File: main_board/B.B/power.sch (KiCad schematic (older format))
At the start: 38 parts

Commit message: konzultace_s_Kubou_01
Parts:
- removed C? (x7): 10uf, Capacitor_SMD:C_0805_2012Metric, symbol Device:C
- removed C? (x3): 2.2uf, Capacitor_SMD:C_0805_2012Metric, symbol Device:C
- removed C? (x4): 22uf, Capacitor_SMD:C_0805_2012Metric, symbol Device:C
- removed C? (x6): 4.7uf, Capacitor_SMD:C_0805_2012Metric, symbol Device:C
- removed C? (x3): 0.1uf, Capacitor_SMD:C_0402_1005Metric, symbol Device:C
- removed L? (x2): 4,7uH, symbol Device:L
- removed L?: 1.5uh, symbol Device:L
- removed R? (x3): 100k, Resistor_SMD:R_0402_1005Metric, symbol Device:R
- removed R?: 33k, Resistor_SMD:R_0402_1005Metric, symbol Device:R
- removed R?: 7.5k, Resistor_SMD:R_0402_1005Metric, symbol Device:R
- removed R?: 150k, Resistor_SMD:R_0402_1005Metric, symbol Device:R
- removed R?: 20k, Resistor_SMD:R_0402_1005Metric, symbol Device:R
- removed R?: 56k, Resistor_SMD:R_0402_1005Metric, symbol Device:R
- removed R?: 10k, Resistor_SMD:R_0402_1005Metric, symbol Device:R
- removed U? (x2): FR9885, Package_TO_SOT_SMD:SOT-23-6, symbol B.B-rescue:FR9885
- removed U?: SY8286A, Package_DFN_QFN:QFN-20-1EP_4x4mm_P0.5mm_EP2.7x2.7mm, symbol B.B-rescue:SY8286A
- added C? (x3): 10uf, Capacitor_SMD:C_0805_2012Metric, symbol Device:C
- added C? (x3): 2.2uf, Capacitor_SMD:C_0805_2012Metric, symbol Device:C
- added C?: 4.7uf, Capacitor_SMD:C_0805_2012Metric, symbol Device:C
- added C? (x4): 22uf, Capacitor_SMD:C_0805_2012Metric, symbol Device:C
- added C?: 100nf, Capacitor_SMD:C_0402_1005Metric, symbol Device:C
- added C?: 10nf, Capacitor_SMD:C_0402_1005Metric, symbol Device:C
- added C?: 47nf, Capacitor_SMD:C_0402_1005Metric, symbol Device:C
- added C?: 10pf, Capacitor_SMD:C_0402_1005Metric, symbol Device:C
- added C?: 1nf, Capacitor_SMD:C_0402_1005Metric, symbol Device:C
- added C?: 1uf, Capacitor_SMD:C_0402_1005Metric, symbol Device:C
- added D? (x2): D_Schottky, symbol Device:D_Schottky
- added L? (x2): 2.2uH, symbol Device:L
- added Q? (x2): Q_NMOS_DSG, symbol Device:Q_NMOS_DSG
- added R?: 150k, Resistor_SMD:R_0402_1005Metric, symbol Device:R
- added R?: 20k, Resistor_SMD:R_0402_1005Metric, symbol Device:R
- added R? (x3): 100k, Resistor_SMD:R_0402_1005Metric, symbol Device:R
- added R?: 33k, Resistor_SMD:R_0402_1005Metric, symbol Device:R
- added R? (x2): 7.5k, Resistor_SMD:R_0402_1005Metric, symbol Device:R
- added R?: 10, Resistor_SMD:R_0402_1005Metric, symbol Device:R
- added R?: 1.5, Resistor_SMD:R_0402_1005Metric, symbol Device:R
- added U?: AOZ1280, Package_TO_SOT_SMD:SOT-23-6, symbol B.B-rescue:AOZ1280
- added U?: FP6296, symbol B.B-rescue:FP6296
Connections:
- net labels removed: 4V, NC, SHUTDOWN_4V, low_power_3V3
- wire segments 105 -> 76
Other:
- note removed: "low power 3V3 output can provide \nmax continuous current 150mA"

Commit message: preparation_to_drawing_PCB
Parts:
- removed D?: D_Schottky, symbol Device:D_Schottky
- removed Q? (x2): Q_NMOS_DSG, symbol Device:Q_NMOS_DSG
- added D?: D_Schottky, BB:DO-214AC, symbol Device:D_Schottky
- added Q? (x2): CJ3134K, Package_TO_SOT_SMD:SOT-23, symbol Transistor_FET:2N7002
- C?: LCSC (none) -> C1525
- C?: value 47nf -> 33nf; LCSC (none) -> C1585
- C?: LCSC (none) -> C32949
- C?: LCSC (none) -> C1523
- C?: LCSC (none) -> C52923
- D?: footprint (none) -> BB:DO-214AC; LCSC (none) -> C22452
- L?: footprint (none) -> BB:SMD-PIND-10.5x11.5x4_2.5x3.0; LCSC (none) -> C149550
- L?: value 2.2uH -> 3.3uH; footprint (none) -> BB:SMD-PIND-12.8x13.5x5_2.0x5.0; LCSC (none) -> C149571
- R?: value 150k -> 100k; LCSC C25755 -> C25741
- R?: value 20k -> 33k; LCSC C25765 -> C25779
- R?: LCSC C25755 -> C25077
- R?: LCSC (none) -> C270642
- U?: footprint (none) -> Package_SO:SOP-8_3.76x4.96mm_P1.27mm; LCSC (none) -> C133888
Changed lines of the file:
@@
 F 0 "L?" V 6590 2350 50  0000 C CNN
 F 1 "2.2uH" V 6499 2350 50  0000 C CNN
-F 2 "" H 6400 2350 50  0001 C CNN
+F 2 "BB:SMD-PIND-10.5x11.5x4_2.5x3.0" H 6400 2350 50  0001 C CNN
 F 3 "~" H 6400 2350 50  0001 C CNN
+F 4 "C149550" V 6400 2350 50  0001 C CNN "LCSC"
 	1    6400 2350
 	0    -1   -1   0
@@
 	4900 2400 4950 2400
 $Comp
-L Device:Q_NMOS_DSG Q?
-U 1 1 5FA82314
-P 4800 2950
-AR Path="/5F9EE529/5FA82314" Ref="Q?"  Part="1"
-AR Path="/5FA9DBB3/5FA82314" Ref="Q?"  Part="1"
-AR Path="/5FA4C94D/5FA82314" Ref="Q?"  Part="1"
-F 0 "Q?" H 5004 2996 50  0000 L CNN
-F 1 "Q_NMOS_DSG" H 5004 2905 50  0000 L CNN
-F 2 "" H 5000 3050 50  0001 C CNN
-F 3 "~" H 4800 2950 50  0001 C CNN
-	1    4800 2950
-	1    0    0    -1
-$EndComp
-$Comp
 L B.B-eagle-import:GND #GND?
 U 1 1 5FA8231A
@@
 F 0 "D?" V 6154 2729 50  0000 L CNN
 F 1 "D_Schottky" V 6245 2729 50  0000 L CNN
-F 2 "" H 6200 2650 50  0001 C CNN
+F 2 "BB:DO-214AC" H 6200 2650 50  0001 C CNN
 F 3 "~" H 6200 2650 50  0001 C CNN
+F 4 "C22452" V 6200 2650 50  0001 C CNN "LCSC"
 	1    6200 2650
 	0    1    1    0
@@
 F 0 "U?" H 5250 4625 50  0000 C CNN
 F 1 "FP6296" H 5250 4534 50  0000 C CNN
-F 2 "" H 5250 4400 50  0001 C CNN
+F 2 "Package_SO:SOP-8_3.76x4.96mm_P1.27mm" H 5250 4400 50  0001 C CNN
 F 3 "" H 5250 4400 50  0001 C CNN
+F 4 "C133888" H 5250 4400 50  0001 C CNN "LCSC"
 	1    5250 4400
 	1    0    0    -1
@@
 AR Path="/5F9AAC80/5FA6804A" Ref="R?"  Part="1"
 F 0 "R?" H 6870 4246 50  0000 L CNN
-F 1 "150k" H 6870 4155 50  0000 L CNN
+F 1 "100k" H 6870 4155 50  0000 L CNN
 F 2 "Resistor_SMD:R_0402_1005Metric" V 6730 4200 50  0001 C CNN
 F 3 "~" H 6800 4200 50  0001 C CNN
-F 4 "C25755" H 6800 4200 50  0001 C CNN "LCSC"
+F 4 "C25741" H 6800 4200 50  0001 C CNN "LCSC"
 	1    6800 4200
 	1    0    0    -1
@@
 AR Path="/5F9AAC80/5FA68052" Ref="R?"  Part="1"
 F 0 "R?" H 6870 4546 50  0000 L CNN
-F 1 "20k" H 6870 4455 50  0000 L CNN
+F 1 "33k" H 6870 4455 50  0000 L CNN
 F 2 "Resistor_SMD:R_0402_1005Metric" V 6730 4500 50  0001 C CNN
 F 3 "~" H 6800 4500 50  0001 C CNN
-F 4 "C25765" H 6800 4500 50  0001 C CNN "LCSC"
+F 4 "C25779" H 6800 4500 50  0001 C CNN "LCSC"
 	1    6800 4500
 	1    0    0    -1
@@
 P 4350 4000
 F 0 "L?" V 4540 4000 50  0000 C CNN
-F 1 "2.2uH" V 4449 4000 50  0000 C CNN
-F 2 "" H 4350 4000 50  0001 C CNN
+F 1 "3.3uH" V 4449 4000 50  0000 C CNN
+F 2 "BB:SMD-PIND-12.8x13.5x5_2.0x5.0" H 4350 4000 50  0001 C CNN
 F 3 "~" H 4350 4000 50  0001 C CNN
+F 4 "C149571" V 4350 4000 50  0001 C CNN "LCSC"
 	1    4350 4000
 	0    -1   -1   0
-$EndComp
-$Comp
-L Device:D_Schottky D?
-U 1 1 5FA8F317
-P 5250 4000
-F 0 "D?" H 5200 3800 50  0000 L CNN
-F 1 "D_Schottky" H 5050 3900 50  0000 L CNN
-F 2 "" H 5250 4000 50  0001 C CNN
-F 3 "~" H 5250 4000 50  0001 C CNN
-	1    5250 4000
-	-1   0    0    1
 $EndComp
 $Comp
@@
 F 2 "Capacitor_SMD:C_0402_1005Metric" H 5888 4250 50  0001 C CNN
 F 3 "~" H 5850 4400 50  0001 C CNN
-F 4 "" V 5850 4400 50  0001 C CNN "LCSC"
+F 4 "C1525" V 5850 4400 50  0001 C CNN "LCSC"
 	1    5850 4400
 	0    1    1    0
@@
 F 2 "Resistor_SMD:R_0402_1005Metric" V 5580 4200 50  0001 C CNN
 F 3 "~" H 5650 4200 50  0001 C CNN
-F 4 "C25755" H 5650 4200 50  0001 C CNN "LCSC"
+F 4 "C25077" H 5650 4200 50  0001 C CNN "LCSC"
 	1    5650 4200
 	1    0    0    -1
@@
 P 6150 4800
 F 0 "C?" V 6100 4700 50  0000 C CNN
-F 1 "47nf" V 6100 4950 50  0000 C CNN
+F 1 "33nf" V 6100 4950 50  0000 C CNN
 F 2 "Capacitor_SMD:C_0402_1005Metric" H 6188 4650 50  0001 C CNN
 F 3 "~" H 6150 4800 50  0001 C CNN
-F 4 "" V 6150 4800 50  0001 C CNN "LCSC"
+F 4 "C1585" V 6150 4800 50  0001 C CNN "LCSC"
 	1    6150 4800
 	0    1    1    0
@@
 F 2 "Capacitor_SMD:C_0402_1005Metric" H 5688 5050 50  0001 C CNN
 F 3 "~" H 5650 5200 50  0001 C CNN
-F 4 "" V 5650 5200 50  0001 C CNN "LCSC"
+F 4 "C32949" V 5650 5200 50  0001 C CNN "LCSC"
 	1    5650 5200
 	-1   0    0    1
@@
 F 2 "Resistor_SMD:R_0402_1005Metric" V 4130 4400 50  0001 C CNN
 F 3 "~" H 4200 4400 50  0001 C CNN
-F 4 "" H 4200 4400 50  0001 C CNN "LCSC"
+F 4 "C270642" H 4200 4400 50  0001 C CNN "LCSC"
 	1    4200 4400
 	1    0    0    -1
@@
 F 2 "Capacitor_SMD:C_0402_1005Metric" H 4238 4550 50  0001 C CNN
 F 3 "~" H 4200 4700 50  0001 C CNN
-F 4 "" V 4200 4700 50  0001 C CNN "LCSC"
+F 4 "C1523" V 4200 4700 50  0001 C CNN "LCSC"
 	1    4200 4700
 	-1   0    0    1
@@
 F 2 "Capacitor_SMD:C_0402_1005Metric" H 4538 4550 50  0001 C CNN
 F 3 "~" H 4500 4700 50  0001 C CNN
-F 4 "" V 4500 4700 50  0001 C CNN "LCSC"
+F 4 "C52923" V 4500 4700 50  0001 C CNN "LCSC"
 	1    4500 4700
 	-1   0    0    1
@@
 $EndComp
 $Comp
-L Device:Q_NMOS_DSG Q?
-U 1 1 5FCDFEE6
-P 4650 5300
-AR Path="/5F9EE529/5FCDFEE6" Ref="Q?"  Part="1"
-AR Path="/5FA9DBB3/5FCDFEE6" Ref="Q?"  Part="1"
-AR Path="/5FA4C94D/5FCDFEE6" Ref="Q?"  Part="1"
-F 0 "Q?" H 4854 5346 50  0000 L CNN
-F 1 "Q_NMOS_DSG" H 4854 5255 50  0000 L CNN
-F 2 "" H 4850 5400 50  0001 C CNN
-F 3 "~" H 4650 5300 50  0001 C CNN
-	1    4650 5300
-	1    0    0    -1
-$EndComp
-$Comp
 L B.B-eagle-import:GND #GND?
 U 1 1 5FCDFEEC
@@
 Wire Wire Line
 	2800 4000 3200 4000
+$Comp
+L Transistor_FET:2N7002 Q?
+U 1 1 5FA8B0DC
+P 4800 2950
+AR Path="/5F77B818/5FA8B0DC" Ref="Q?"  Part="1"
+AR Path="/5FA4C94D/5FA8B0DC" Ref="Q?"  Part="1"
+F 0 "Q?" H 5004 2996 50  0000 L CNN
+F 1 "CJ3134K" H 5004 2905 50  0000 L CNN
+F 2 "Package_TO_SOT_SMD:SOT-23" H 5000 2875 50  0001 L CIN
+F 3 "https://datasheet.lcsc.com/szlcsc/Changjiang-Electronics-Tech-CJ-CJ3134K_C110100.pdf" H 4800 2950 50  0001 L CNN
+F 4 "C110100" H 4800 2950 50  0001 C CNN "LCSC"
+	1    4800 2950
+	1    0    0    -1
+$EndComp
+$Comp
+L Transistor_FET:2N7002 Q?
+U 1 1 5FA8CB53
+P 4650 5300
+AR Path="/5F77B818/5FA8CB53" Ref="Q?"  Part="1"
+AR Path="/5FA4C94D/5FA8CB53" Ref="Q?"  Part="1"
+F 0 "Q?" H 4854 5346 50  0000 L CNN
+F 1 "CJ3134K" H 4854 5255 50  0000 L CNN
+F 2 "Package_TO_SOT_SMD:SOT-23" H 4850 5225 50  0001 L CIN
+F 3 "https://datasheet.lcsc.com/szlcsc/Changjiang-Electronics-Tech-CJ-CJ3134K_C110100.pdf" H 4650 5300 50  0001 L CNN
+F 4 "C110100" H 4650 5300 50  0001 C CNN "LCSC"
+	1    4650 5300
+	1    0    0    -1
+$EndComp
+$Comp
+L Device:D_Schottky D?
+U 1 1 5FB0ACB2
+P 5250 4000
+F 0 "D?" H 5200 3800 50  0000 L CNN
+F 1 "D_Schottky" H 5050 3900 50  0000 L CNN
+F 2 "BB:DO-214AC" H 5250 4000 50  0001 C CNN
+F 3 "~" H 5250 4000 50  0001 C CNN
+F 4 "C22452" V 5250 4000 50  0001 C CNN "LCSC"
+	1    5250 4000
+	-1   0    0    1
+$EndComp
 $EndSCHEMATC

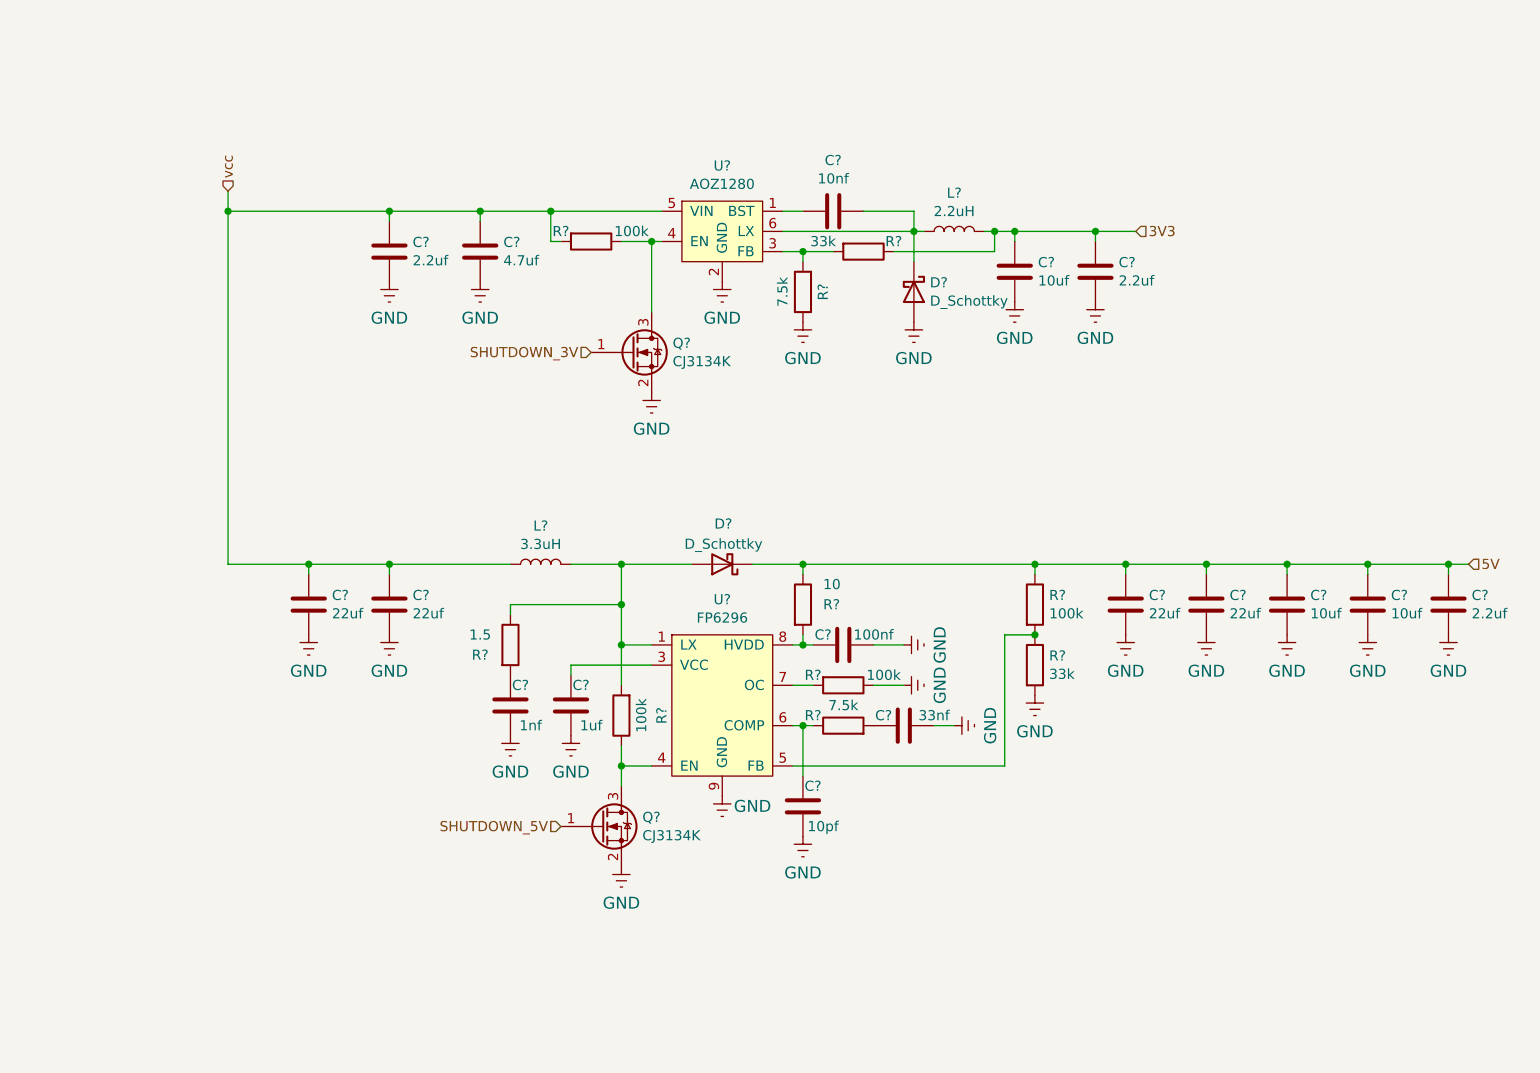
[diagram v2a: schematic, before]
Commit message: complete_preparation_to_drawing_PCB
footprint for all component and LCSC code for everything for mounting in JLCPCB
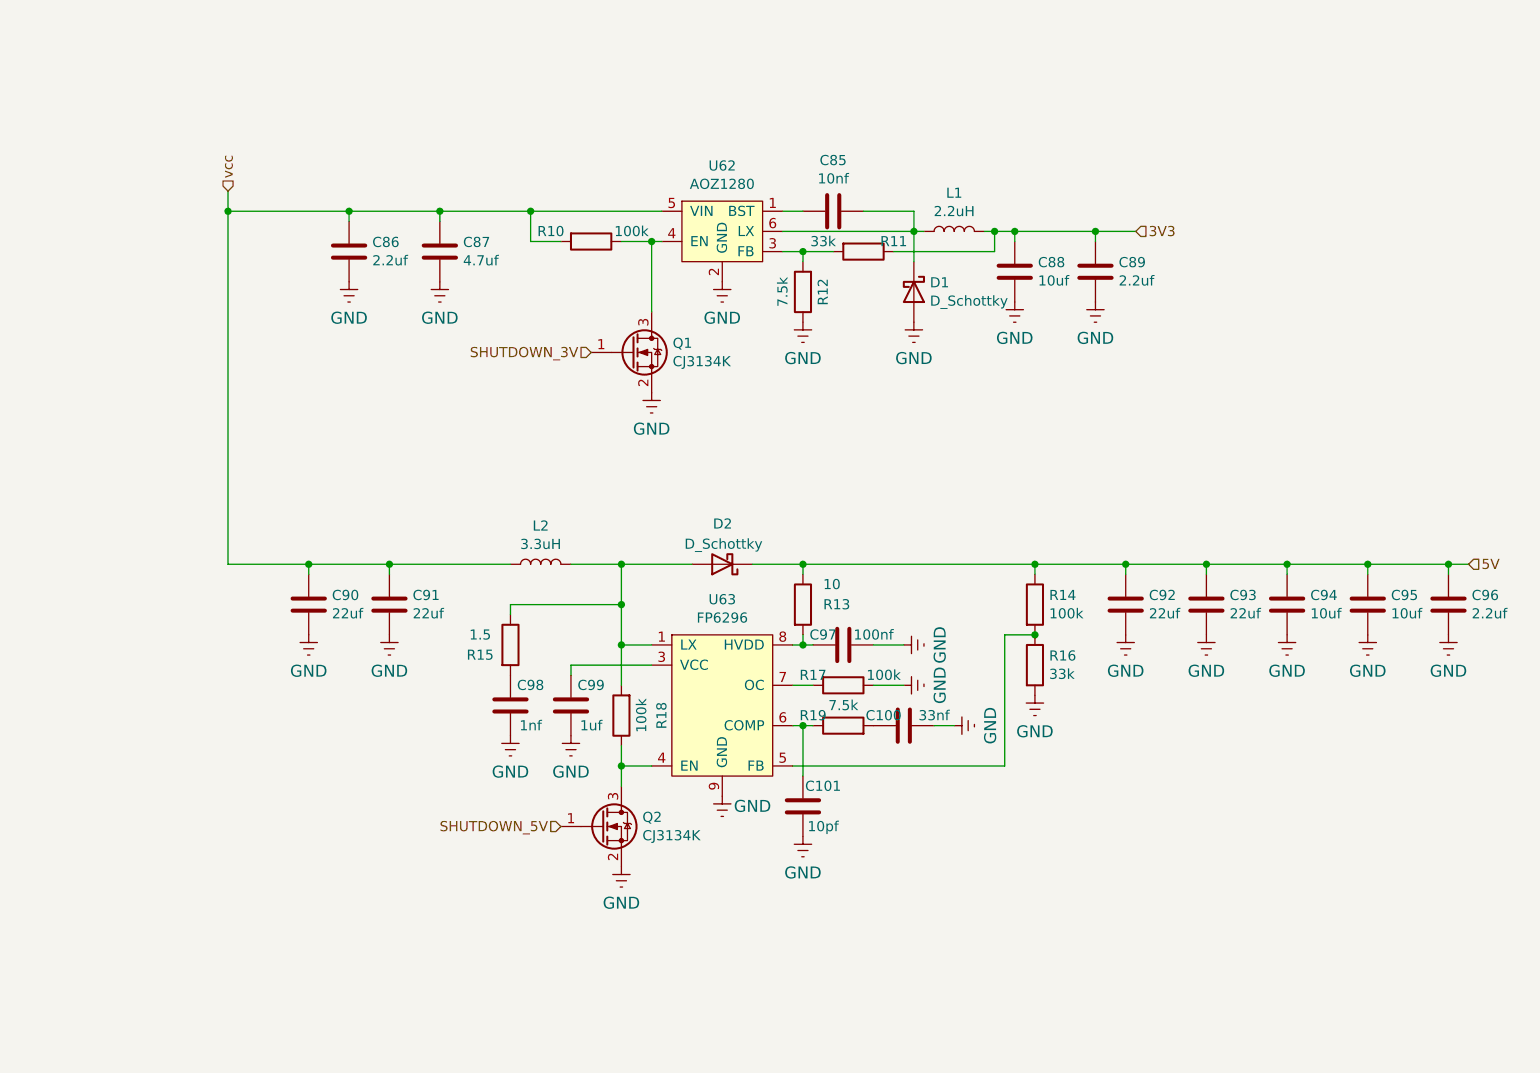
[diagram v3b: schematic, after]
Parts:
- gave numbers to parts that had none: 35
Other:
- moved on the sheet: C86, C87

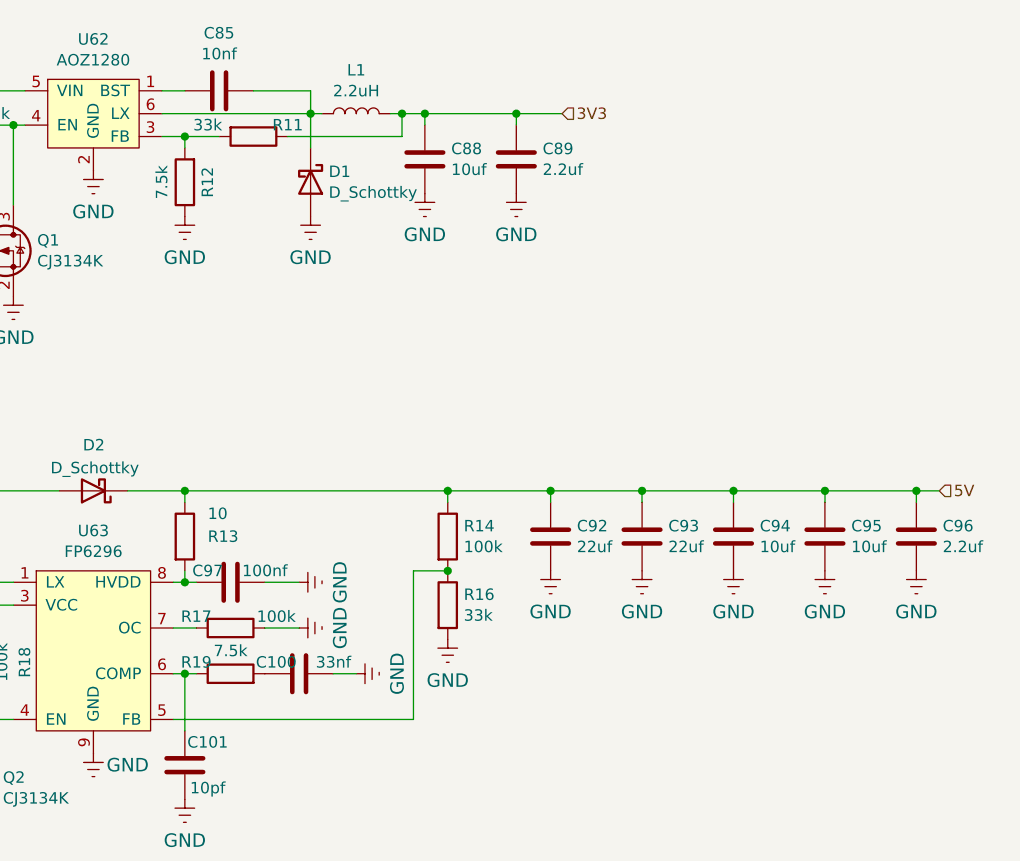
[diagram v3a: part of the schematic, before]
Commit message: optimalizace_kondenzatoru
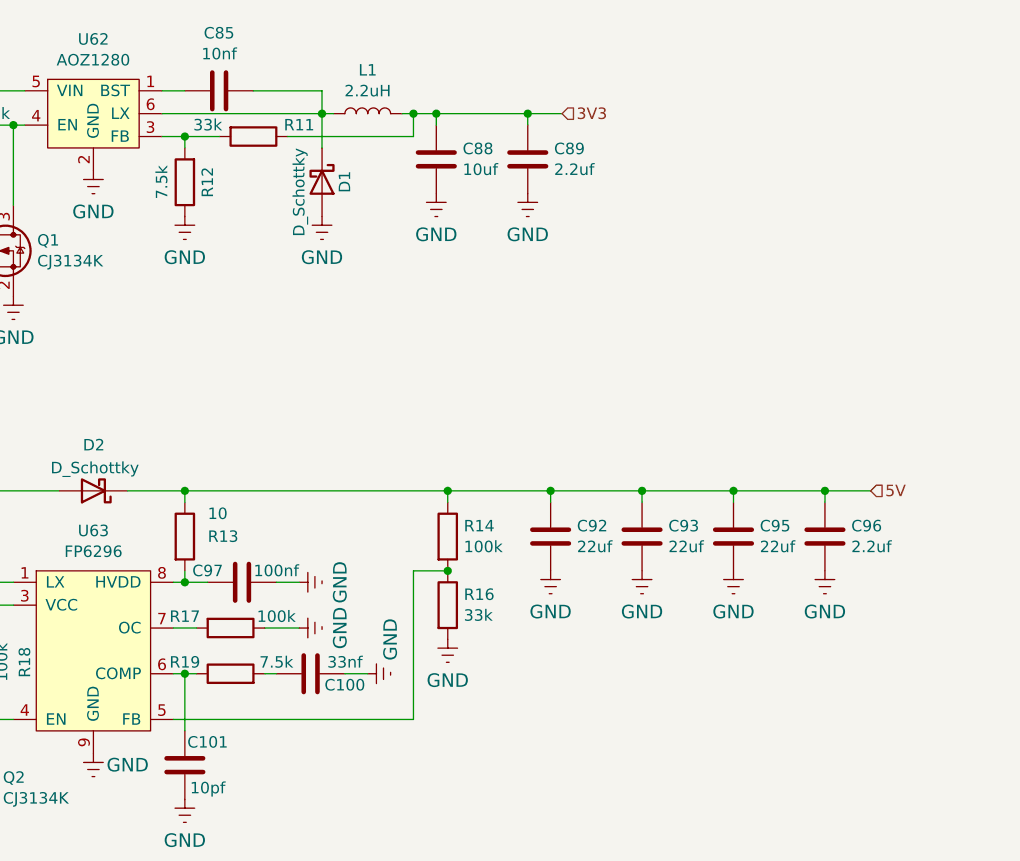
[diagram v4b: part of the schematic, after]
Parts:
- removed C94: 10uf, Capacitor_SMD:C_0805_2012Metric, symbol Device:C
- C95: value 10uf -> 22uf; LCSC C15850 -> C45783
- U63: footprint Package_SO:SOP-8_3.76x4.96mm_P1.27mm -> BB:SOP-8+1_3.76x4.96mm_P1.27mm
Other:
- moved on the sheet: C100, C88, C89, C96, C97, D1, L1
